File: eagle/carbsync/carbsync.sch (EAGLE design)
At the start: 30 parts, among them Q1 IRLML6344

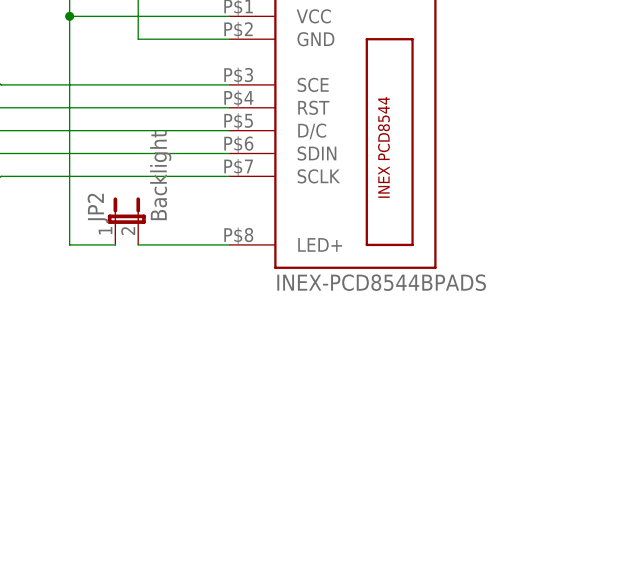
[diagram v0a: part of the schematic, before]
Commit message: update & shrink board a little
Still uses a MOSFET for reverse voltage protection,
but I'm pretty sure it won't work.
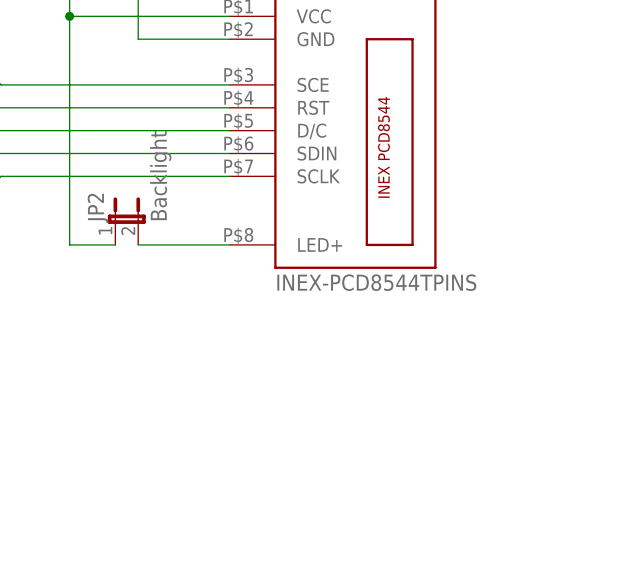
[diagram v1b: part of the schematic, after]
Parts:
- U$7: value INEX-PCD8544BPADS -> INEX-PCD8544TPINS; device synfinatic:INEX-PCD8544BPADS -> synfinatic:INEX-PCD8544TPINS
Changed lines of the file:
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@@
 <part name="U$5" library="teensy" deviceset="TEENSY" device=""/>
 <part name="U$1" library="synfinatic" deviceset="MPXV5050V" device=""/>
-<part name="U$7" library="synfinatic" deviceset="INEX-PCD8544" device="BPADS" value="INEX-PCD8544BPADS"/>
+<part name="U$7" library="synfinatic" deviceset="INEX-PCD8544" device="TPINS" value="INEX-PCD8544TPINS"/>
 <part name="SUPPLY2" library="SparkFun-Aesthetics" deviceset="5V" device=""/>
 <part name="GND2" library="SparkFun-Aesthetics" deviceset="GND" device=""/>

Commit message: remove mosfet, switch to 2-DIP instead of jumpers
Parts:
- removed D1: 10V Z, adafruit:DIODESOD-123
- removed JP2: Backlight, jumper:JP1E
- removed JP3: 2/4 Cyl, jumper:JP1E
- removed Q1: IRLML6344, synfinatic:IRLML6344
- removed R1: 13.3k, resistor:R-US_M0805
- added U$9: CT-219-X-MST, synfinatic:CT-219-X-MST
- U$10: device SteelCaveRobotics-Power:MCP1825SOT-223-3 -> synfinatic:MCP1825SOT-223-3
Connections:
- removed net -: BAT1.-, Q1.D
- removed net N$10: JP3.2, U$5._D0
- removed net N$6: JP2.2, U$7.LED+
- removed net N$8: D1.C, Q1.G, R1.1
- new net 4CYL: U$5._D0, U$9.P$2
- new net LED: U$7.LED+, U$9.P$4
- net 3.3V: now also U$9.P$3; no longer JP2.1
- net GND: now also S1.1, U$10.GND@1, U$9.P$1; no longer D1.A, JP3.1, Q1.S
- net N$7: now also BAT1.-; no longer R1.2
- net VBATT: no longer S1.1
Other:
- moved on the sheet: S1
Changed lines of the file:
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@@
 <part name="U$6" library="microbuilder" deviceset="74HC4050D" device="" value="74HC4050D"/>
 <part name="GND6" library="SparkFun-Aesthetics" deviceset="GND" device=""/>
-<part name="JP2" library="jumper" deviceset="JP1E" device="" value="Backlight"/>
-<part name="GND9" library="SparkFun-Aesthetics" deviceset="GND" device=""/>
 <part name="U$8" library="synfinatic" deviceset="POLOLU-DC-3PIN" device="U1V10F5-5V-DC-UP"/>
 <part name="GND1" library="SparkFun-Aesthetics" deviceset="GND" device=""/>
 <part name="SUPPLY1" library="SparkFun-Aesthetics" deviceset="5V" device=""/>
-<part name="Q1" library="synfinatic" deviceset="IRLML6344" device=""/>
-<part name="D1" library="adafruit" deviceset="DIODE" device="SOD-123" value="10V Z"/>
-<part name="R1" library="resistor" deviceset="R-US_" device="M0805" value="13.3k"/>
 <part name="GND10" library="SparkFun-Aesthetics" deviceset="GND" device=""/>
-<part name="U$10" library="SteelCaveRobotics-Power" deviceset="MCP1825" device="SOT-223-3"/>
+<part name="U$10" library="synfinatic" deviceset="MCP1825" device="SOT-223-3"/>
 <part name="C1" library="resistor" deviceset="C-US" device="C0805" value="1uF"/>
 <part name="C2" library="resistor" deviceset="C-US" device="C0805" value="4.7uF"/>
@@
 <part name="C13" library="resistor" deviceset="C-US" device="C0805" value=".01uF"/>
 <part name="C14" library="resistor" deviceset="C-US" device="C0603" value="470pF"/>
-<part name="JP3" library="jumper" deviceset="JP1E" device="" value="2/4 Cyl"/>
 <part name="BAT1" library="synfinatic" deviceset="BATTERY" device="KEYSTONE-2462-2-AA" value="2xAA"/>
+<part name="U$9" library="synfinatic" deviceset="CT-219-X-MST" device=""/>
+<part name="SUPPLY10" library="SparkFun-Aesthetics" deviceset="3.3V" device=""/>
+<part name="GND12" library="SparkFun-Aesthetics" deviceset="GND" device=""/>
 </parts>
 <sheets>
@@
 <instance part="U$6" gate="G$1" x="111.76" y="38.1"/>
 <instance part="GND6" gate="1" x="96.52" y="10.16"/>
-<instance part="JP2" gate="A" x="139.7" y="30.48"/>
-<instance part="GND9" gate="1" x="10.16" y="73.66"/>
 <instance part="U$8" gate="G$1" x="167.64" y="91.44"/>
 <instance part="GND1" gate="1" x="177.8" y="78.74"/>
 <instance part="SUPPLY1" gate="G$1" x="193.04" y="88.9"/>
-<instance part="Q1" gate="G$1" x="-45.72" y="71.12"/>
-<instance part="D1" gate="G$1" x="-58.42" y="58.42" rot="R90"/>
-<instance part="R1" gate="G$1" x="-58.42" y="78.74" rot="R90"/>
-<instance part="GND10" gate="1" x="-50.8" y="45.72"/>
+<instance part="GND10" gate="1" x="-25.4" y="68.58"/>
 <instance part="U$10" gate="G$1" x="-33.02" y="17.78"/>
 <instance part="C1" gate="G$1" x="-15.24" y="5.08"/>
@@
 <instance part="SUPPLY7" gate="G$1" x="134.62" y="63.5"/>
 <instance part="SUPPLY13" gate="G$1" x="96.52" y="63.5"/>
-<instance part="S1" gate="G$1" x="-55.88" y="93.98" rot="R90"/>
+<instance part="S1" gate="G$1" x="-30.48" y="78.74" rot="R270"/>
 <instance part="C3" gate="G$1" x="-55.88" y="121.92"/>
 <instance part="C4" gate="G$1" x="-45.72" y="121.92"/>
@@
 <instance part="C13" gate="G$1" x="149.86" y="121.92"/>
 <instance part="C14" gate="G$1" x="157.48" y="132.08"/>
-<instance part="JP3" gate="A" x="10.16" y="86.36"/>
 <instance part="BAT1" gate="G$1" x="-27.94" y="91.44" rot="R270"/>
+<instance part="U$9" gate="DIP$1" x="109.22" y="83.82"/>
+<instance part="SUPPLY10" gate="G$1" x="96.52" y="93.98"/>
+<instance part="GND12" gate="1" x="96.52" y="76.2"/>
 </instances>
 <busses>
@@
 </segment>
 <segment>
-<wire x1="10.16" y1="83.82" x2="10.16" y2="76.2" width="0.1524" layer="91"/>
-<pinref part="GND9" gate="1" pin="GND"/>
-<pinref part="JP3" gate="A" pin="1"/>
-</segment>
-<segment>
 <pinref part="U$8" gate="G$1" pin="GND"/>
 <wire x1="177.8" y1="86.36" x2="177.8" y2="81.28" width="0.1524" layer="91"/>
@@
 </segment>
 <segment>
-<pinref part="D1" gate="G$1" pin="A"/>
-<wire x1="-58.42" y1="55.88" x2="-58.42" y2="53.34" width="0.1524" layer="91"/>
-<wire x1="-58.42" y1="53.34" x2="-50.8" y2="53.34" width="0.1524" layer="91"/>
-<wire x1="-50.8" y1="53.34" x2="-43.18" y2="53.34" width="0.1524" layer="91"/>
-<wire x1="-43.18" y1="53.34" x2="-43.18" y2="66.04" width="0.1524" layer="91"/>
-<pinref part="Q1" gate="G$1" pin="S"/>
-<wire x1="-50.8" y1="53.34" x2="-50.8" y2="48.26" width="0.1524" layer="91"/>
-<junction x="-50.8" y="53.34"/>
-<pinref part="GND10" gate="1" pin="GND"/>
-</segment>
-<segment>
 <pinref part="C2" gate="G$1" pin="2"/>
-<wire x1="-50.8" y1="0" x2="-33.02" y2="0" width="0.1524" layer="91"/>
-<wire x1="-33.02" y1="0" x2="-15.24" y2="0" width="0.1524" layer="91"/>
+<wire x1="-50.8" y1="0" x2="-35.56" y2="0" width="0.1524" layer="91"/>
+<wire x1="-35.56" y1="0" x2="-33.02" y2="0" width="0.1524" layer="91"/>
+<wire x1="-33.02" y1="0" x2="-30.48" y2="0" width="0.1524" layer="91"/>
 <pinref part="C1" gate="G$1" pin="2"/>
-<pinref part="U$10" gate="G$1" pin="GND@2"/>
-<wire x1="-33.02" y1="10.16" x2="-33.02" y2="0" width="0.1524" layer="91"/>
 <junction x="-33.02" y="0"/>
 <pinref part="GND11" gate="1" pin="GND"/>
+<pinref part="U$10" gate="G$1" pin="GND@1"/>
+<wire x1="-30.48" y1="0" x2="-15.24" y2="0" width="0.1524" layer="91"/>
+<wire x1="-35.56" y1="10.16" x2="-35.56" y2="0" width="0.1524" layer="91"/>
+<junction x="-35.56" y="0"/>
+<pinref part="U$10" gate="G$1" pin="GND@2"/>
+<wire x1="-30.48" y1="10.16" x2="-30.48" y2="0" width="0.1524" layer="91"/>
+<junction x="-30.48" y="0"/>
 </segment>
 <segment>
@@
 <pinref part="U$4" gate="G$1" pin="GND"/>
 </segment>
+<segment>
+<pinref part="S1" gate="G$1" pin="1"/>
+<pinref part="GND10" gate="1" pin="GND"/>
+<wire x1="-25.4" y1="73.66" x2="-25.4" y2="71.12" width="0.1524" layer="91"/>
+</segment>
+<segment>
+<pinref part="U$9" gate="DIP$1" pin="P$1"/>
+<wire x1="104.14" y1="81.28" x2="96.52" y2="81.28" width="0.1524" layer="91"/>
+<wire x1="96.52" y1="81.28" x2="96.52" y2="78.74" width="0.1524" layer="91"/>
+<pinref part="GND12" gate="1" pin="GND"/>
+</segment>
 </net>
 <net name="5V" class="0">
@@
 </segment>
 </net>
-<net name="N$6" class="0">
+<net name="LED" class="0">
 <segment>
 <pinref part="U$7" gate="G$1" pin="LED+"/>
 <wire x1="152.4" y1="27.94" x2="142.24" y2="27.94" width="0.1524" layer="91"/>
-<pinref part="JP2" gate="A" pin="2"/>
-</segment>
-</net>
-<net name="N$10" class="0">
-<segment>
-<pinref part="U$5" gate="G$1" pin="_D0"/>
-<wire x1="12.7" y1="83.82" x2="25.4" y2="83.82" width="0.1524" layer="91"/>
-<pinref part="JP3" gate="A" pin="2"/>
-</segment>
-</net>
-<net name="N$8" class="0">
-<segment>
-<pinref part="R1" gate="G$1" pin="1"/>
-<wire x1="-58.42" y1="73.66" x2="-58.42" y2="68.58" width="0.1524" layer="91"/>
-<pinref part="D1" gate="G$1" pin="C"/>
-<wire x1="-58.42" y1="68.58" x2="-58.42" y2="60.96" width="0.1524" layer="91"/>
-<wire x1="-58.42" y1="68.58" x2="-48.26" y2="68.58" width="0.1524" layer="91"/>
-<junction x="-58.42" y="68.58"/>
-<pinref part="Q1" gate="G$1" pin="G"/>
+<label x="142.24" y="27.94" size="1.778" layer="95" rot="R180" xref="yes"/>
+</segment>
+<segment>
+<pinref part="U$9" gate="DIP$1" pin="P$4"/>
+<wire x1="119.38" y1="88.9" x2="124.46" y2="88.9" width="0.1524" layer="91"/>
+<label x="124.46" y="88.9" size="1.778" layer="95" xref="yes"/>
 </segment>
 </net>
@@
 </segment>
 <segment>
-<pinref part="S1" gate="G$1" pin="1"/>
-<wire x1="-60.96" y1="99.06" x2="-60.96" y2="104.14" width="0.1524" layer="91"/>
-<wire x1="-60.96" y1="104.14" x2="-27.94" y2="104.14" width="0.1524" layer="91"/>
 <pinref part="BAT1" gate="G$1" pin="+"/>
 <wire x1="-27.94" y1="104.14" x2="-27.94" y2="96.52" width="0.1524" layer="91"/>
-<junction x="-27.94" y="104.14"/>
 <label x="-27.94" y="104.14" size="1.778" layer="95" xref="yes"/>
-</segment>
-</net>
-<net name="N$7" class="0">
-<segment>
-<pinref part="R1" gate="G$1" pin="2"/>
-<wire x1="-58.42" y1="88.9" x2="-58.42" y2="83.82" width="0.1524" layer="91"/>
-<pinref part="S1" gate="G$1" pin="2"/>
-</segment>
-</net>
-<net name="-" class="0">
-<segment>
-<pinref part="Q1" gate="G$1" pin="D"/>
-<wire x1="-43.18" y1="76.2" x2="-43.18" y2="83.82" width="0.1524" layer="91"/>
-<pinref part="BAT1" gate="G$1" pin="-"/>
-<wire x1="-27.94" y1="86.36" x2="-27.94" y2="83.82" width="0.1524" layer="91"/>
-<wire x1="-27.94" y1="83.82" x2="-43.18" y2="83.82" width="0.1524" layer="91"/>
 </segment>
 </net>
@@
 <pinref part="SUPPLY7" gate="G$1" pin="3.3V"/>
 <wire x1="134.62" y1="53.34" x2="134.62" y2="63.5" width="0.1524" layer="91"/>
-<pinref part="JP2" gate="A" pin="1"/>
-<wire x1="139.7" y1="27.94" x2="134.62" y2="27.94" width="0.1524" layer="91"/>
-<wire x1="134.62" y1="27.94" x2="134.62" y2="53.34" width="0.1524" layer="91"/>
-<junction x="134.62" y="53.34"/>
-</segment>
-</net>
+</segment>
+<segment>
+<pinref part="U$9" gate="DIP$1" pin="P$3"/>
+<wire x1="104.14" y1="88.9" x2="96.52" y2="88.9" width="0.1524" layer="91"/>
+<wire x1="96.52" y1="88.9" x2="96.52" y2="93.98" width="0.1524" layer="91"/>
+<pinref part="SUPPLY10" gate="G$1" pin="3.3V"/>
+</segment>
+</net>
+<net name="N$7" class="0">
+<segment>
+<pinref part="BAT1" gate="G$1" pin="-"/>
+<pinref part="S1" gate="G$1" pin="2"/>
+<wire x1="-27.94" y1="86.36" x2="-27.94" y2="83.82" width="0.1524" layer="91"/>
+</segment>
+</net>
+<net name="4CYL" class="0">
+<segment>
+<pinref part="U$9" gate="DIP$1" pin="P$2"/>
+<wire x1="119.38" y1="81.28" x2="124.46" y2="81.28" width="0.1524" layer="91"/>
+<label x="124.46" y="81.28" size="1.778" layer="95" xref="yes"/>
+</segment>
+<segment>
+<pinref part="U$5" gate="G$1" pin="_D0"/>
+<wire x1="12.7" y1="83.82" x2="25.4" y2="83.82" width="0.1524" layer="91"/>
+<label x="12.7" y="83.82" size="1.778" layer="95" rot="R180" xref="yes"/>
+</segment>
+</net>

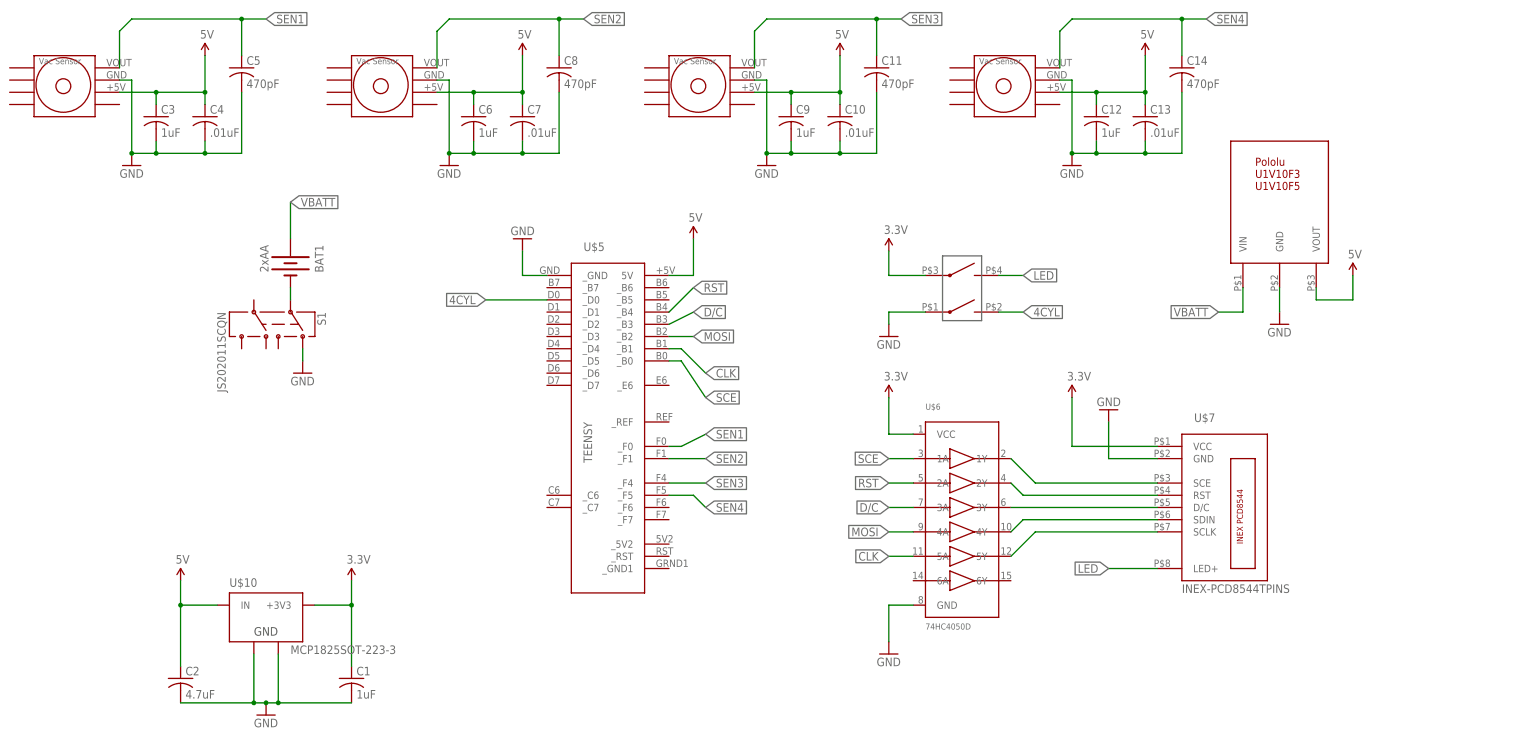
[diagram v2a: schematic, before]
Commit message: basic 3.5x2.5" board design
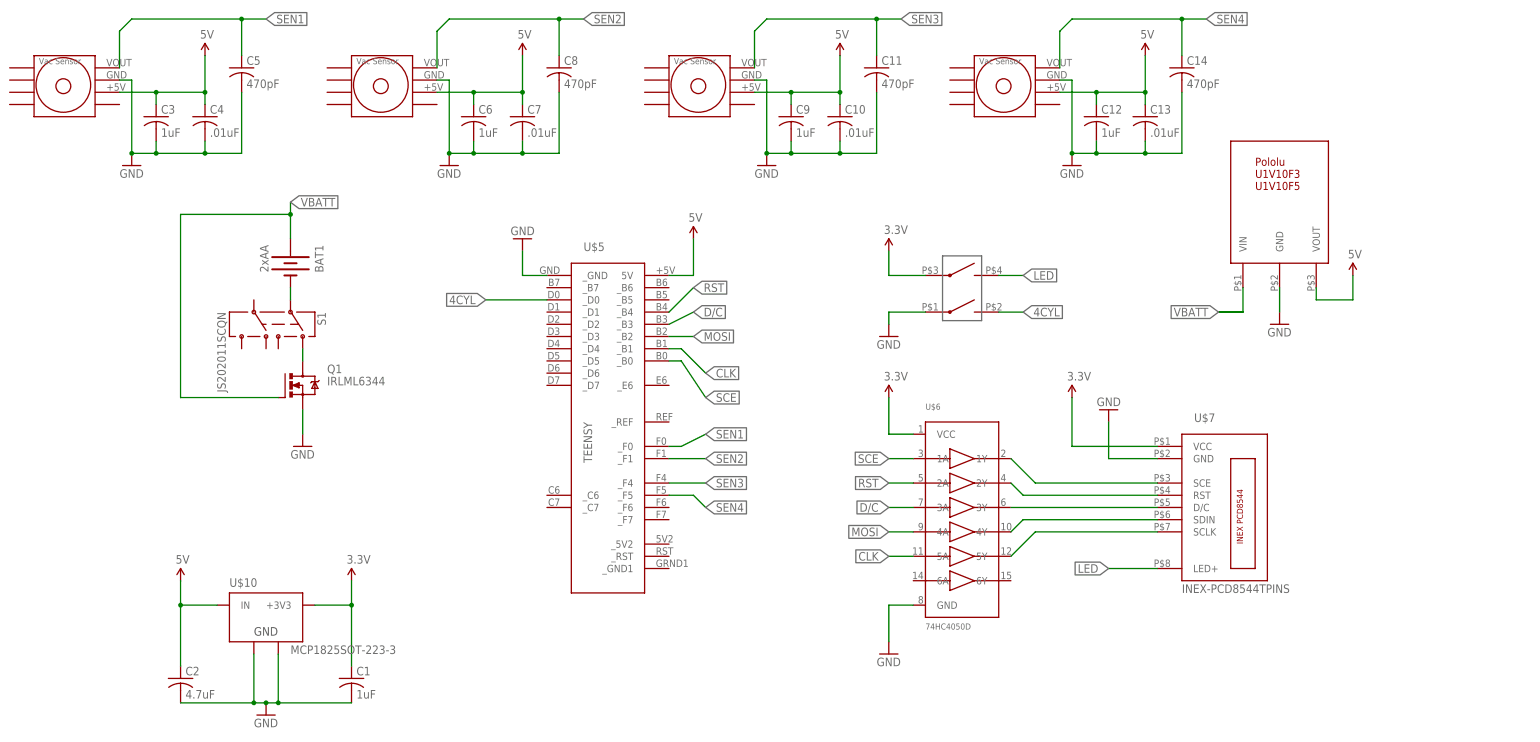
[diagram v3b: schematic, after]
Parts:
- added Q1: IRLML6344, synfinatic:IRLML6344
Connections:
- new net N$6: Q1.D, S1.1
- net GND: now also Q1.S; no longer S1.1
- net VBATT: now also Q1.G
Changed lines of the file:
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@@
 <part name="SUPPLY10" library="SparkFun-Aesthetics" deviceset="3.3V" device=""/>
 <part name="GND12" library="SparkFun-Aesthetics" deviceset="GND" device=""/>
+<part name="Q1" library="synfinatic" deviceset="IRLML6344" device=""/>
 </parts>
 <sheets>
@@
 <instance part="GND1" gate="1" x="177.8" y="78.74"/>
 <instance part="SUPPLY1" gate="G$1" x="193.04" y="88.9"/>
-<instance part="GND10" gate="1" x="-25.4" y="68.58"/>
+<instance part="GND10" gate="1" x="-25.4" y="53.34"/>
 <instance part="U$10" gate="G$1" x="-33.02" y="17.78"/>
 <instance part="C1" gate="G$1" x="-15.24" y="5.08"/>
@@
 <instance part="SUPPLY10" gate="G$1" x="96.52" y="93.98"/>
 <instance part="GND12" gate="1" x="96.52" y="76.2"/>
+<instance part="Q1" gate="G$1" x="-27.94" y="66.04"/>
 </instances>
 <busses>
@@
 </segment>
 <segment>
-<pinref part="S1" gate="G$1" pin="1"/>
-<pinref part="GND10" gate="1" pin="GND"/>
-<wire x1="-25.4" y1="73.66" x2="-25.4" y2="71.12" width="0.1524" layer="91"/>
-</segment>
-<segment>
 <pinref part="U$9" gate="DIP$1" pin="P$1"/>
 <wire x1="104.14" y1="81.28" x2="96.52" y2="81.28" width="0.1524" layer="91"/>
 <wire x1="96.52" y1="81.28" x2="96.52" y2="78.74" width="0.1524" layer="91"/>
 <pinref part="GND12" gate="1" pin="GND"/>
+</segment>
+<segment>
+<pinref part="Q1" gate="G$1" pin="S"/>
+<pinref part="GND10" gate="1" pin="GND"/>
+<wire x1="-25.4" y1="60.96" x2="-25.4" y2="55.88" width="0.1524" layer="91"/>
 </segment>
 </net>
@@
 <wire x1="170.18" y1="81.28" x2="165.1" y2="81.28" width="0.1524" layer="91"/>
 <label x="165.1" y="81.28" size="1.778" layer="95" rot="R180" xref="yes"/>
+<wire x1="170.18" y1="81.28" x2="165.1" y2="81.28" width="0.1524" layer="91"/>
 </segment>
 <segment>
 <pinref part="BAT1" gate="G$1" pin="+"/>
-<wire x1="-27.94" y1="104.14" x2="-27.94" y2="96.52" width="0.1524" layer="91"/>
+<wire x1="-27.94" y1="104.14" x2="-27.94" y2="101.6" width="0.1524" layer="91"/>
 <label x="-27.94" y="104.14" size="1.778" layer="95" xref="yes"/>
+<pinref part="Q1" gate="G$1" pin="G"/>
+<wire x1="-27.94" y1="101.6" x2="-27.94" y2="96.52" width="0.1524" layer="91"/>
+<wire x1="-30.48" y1="63.5" x2="-50.8" y2="63.5" width="0.1524" layer="91"/>
+<wire x1="-50.8" y1="63.5" x2="-50.8" y2="101.6" width="0.1524" layer="91"/>
+<wire x1="-50.8" y1="101.6" x2="-27.94" y2="101.6" width="0.1524" layer="91"/>
+<junction x="-27.94" y="101.6"/>
 </segment>
 </net>
@@
 </segment>
 </net>
+<net name="N$6" class="0">
+<segment>
+<pinref part="S1" gate="G$1" pin="1"/>
+<pinref part="Q1" gate="G$1" pin="D"/>
+<wire x1="-25.4" y1="73.66" x2="-25.4" y2="71.12" width="0.1524" layer="91"/>
+</segment>
+</net>
